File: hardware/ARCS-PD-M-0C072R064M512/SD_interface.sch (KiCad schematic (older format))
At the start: 8 parts

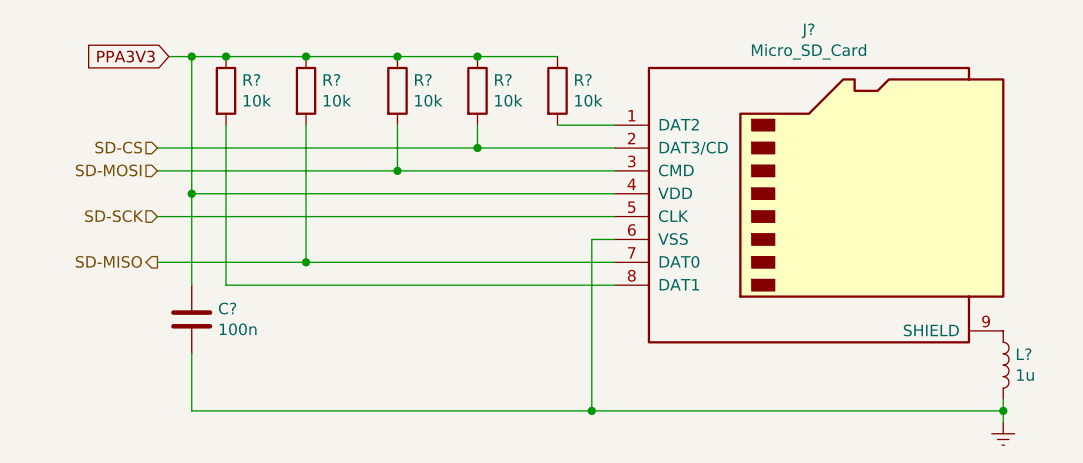
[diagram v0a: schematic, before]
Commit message: Create cards for input and output interface.
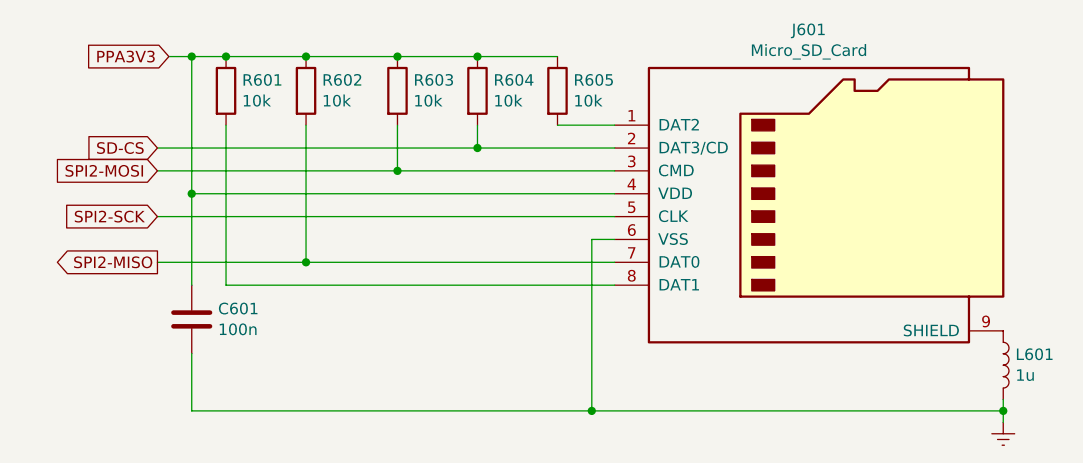
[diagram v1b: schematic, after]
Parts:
- gave numbers to parts that had none: 8
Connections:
- net SD-MISO renamed SPI2-MISO
- net SD-MOSI renamed SPI2-MOSI
- net SD-SCK renamed SPI2-SCK
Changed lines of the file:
@@
 $EndDescr
 $Comp
-L Connector:Micro_SD_Card J?
+L Connector:Micro_SD_Card J601
 U 1 1 5CCB2F0A
 P 7000 3550
-F 0 "J?" H 6950 4267 50  0000 C CNN
+F 0 "J601" H 6950 4267 50  0000 C CNN
 F 1 "Micro_SD_Card" H 6950 4176 50  0000 C CNN
 F 2 "" H 8150 3850 50  0001 C CNN
@@
 $EndComp
 $Comp
-L Device:L L?
+L Device:L L601
 U 1 1 5CCB2F51
 P 7800 4300
-F 0 "L?" H 7853 4346 50  0000 L CNN
+F 0 "L601" H 7853 4346 50  0000 L CNN
 F 1 "1u" H 7853 4255 50  0000 L CNN
 F 2 "" H 7800 4300 50  0001 C CNN
@@
 $EndComp
 $Comp
-L power:Earth #PWR?
+L power:Earth #PWR0601
 U 1 1 5CCB3027
 P 7800 4550
-F 0 "#PWR?" H 7800 4300 50  0001 C CNN
+F 0 "#PWR0601" H 7800 4300 50  0001 C CNN
 F 1 "Earth" H 7800 4400 50  0001 C CNN
 F 2 "" H 7800 4550 50  0001 C CNN
@@
 $EndComp
 $Comp
-L Device:R R?
+L Device:R R605
 U 1 1 5CCB3064
 P 5850 3100
-F 0 "R?" H 5920 3146 50  0000 L CNN
+F 0 "R605" H 5920 3146 50  0000 L CNN
 F 1 "10k" H 5920 3055 50  0000 L CNN
 F 2 "" V 5780 3100 50  0001 C CNN
@@
 $EndComp
 $Comp
-L Device:R R?
+L Device:R R604
 U 1 1 5CCB30DD
 P 5500 3100
-F 0 "R?" H 5570 3146 50  0000 L CNN
+F 0 "R604" H 5570 3146 50  0000 L CNN
 F 1 "10k" H 5570 3055 50  0000 L CNN
 F 2 "" V 5430 3100 50  0001 C CNN
@@
 $EndComp
 $Comp
-L Device:R R?
+L Device:R R603
 U 1 1 5CCB30FF
 P 5150 3100
-F 0 "R?" H 5220 3146 50  0000 L CNN
+F 0 "R603" H 5220 3146 50  0000 L CNN
 F 1 "10k" H 5220 3055 50  0000 L CNN
 F 2 "" V 5080 3100 50  0001 C CNN
@@
 $EndComp
 $Comp
-L Device:R R?
+L Device:R R602
 U 1 1 5CCB3123
 P 4750 3100
-F 0 "R?" H 4820 3146 50  0000 L CNN
+F 0 "R602" H 4820 3146 50  0000 L CNN
 F 1 "10k" H 4820 3055 50  0000 L CNN
 F 2 "" V 4680 3100 50  0001 C CNN
@@
 $EndComp
 $Comp
-L Device:R R?
+L Device:R R601
 U 1 1 5CCB314F
 P 4400 3100
-F 0 "R?" H 4470 3146 50  0000 L CNN
+F 0 "R601" H 4470 3146 50  0000 L CNN
 F 1 "10k" H 4470 3055 50  0000 L CNN
 F 2 "" V 4330 3100 50  0001 C CNN
@@
 	4400 3950 6100 3950
 $Comp
-L Device:C C?
+L Device:C C601
 U 1 1 5CCB3F71
 P 4250 4100
-F 0 "C?" H 4365 4146 50  0000 L CNN
+F 0 "C601" H 4365 4146 50  0000 L CNN
 F 1 "100n" H 4365 4055 50  0000 L CNN
 F 2 "" H 4288 3950 50  0001 C CNN
@@
 Wire Wire Line
 	6000 4500 4250 4500
-Text HLabel 4100 3350 0    50   Input ~ 0
+Text GLabel 4100 3450 0    50   Input ~ 0
+SPI2-MOSI
+Text GLabel 4100 3850 0    50   Output ~ 0
+SPI2-MISO
+Text GLabel 4100 3650 0    50   Input ~ 0
+SPI2-SCK
+Text GLabel 4100 3350 0    50   Input ~ 0
 SD-CS
-Text HLabel 4100 3450 0    50   Input ~ 0
-SD-MOSI
-Text HLabel 4100 3650 0    50   Input ~ 0
-SD-SCK
-Text HLabel 4100 3850 0    50   Output ~ 0
-SD-MISO
 $EndSCHEMATC
